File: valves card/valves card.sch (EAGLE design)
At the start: 68 parts, among them J1 09231486921, J2 TBP02R1-381-14BE, Q1 IRLZ44NSTRLPBF, Q11 IRLZ44NSTRLPBF, Q13 IRLZ44NSTRLPBF, Q15 IRLZ44NSTRLPBF, Q17 IRLZ44NSTRLPBF, Q19 IRLZ44NSTRLPBF, Q21 IRLZ44NSTRLPBF, Q23 IRLZ44NSTRLPBF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

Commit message: added cam data
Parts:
- Q1, Q11, Q13, Q15, Q17, Q19, Q21, Q23, Q3, Q5, Q7, Q9: device m_transistor:STD45NF75 -> BUK9214-30A,118:BUK9214-30A-118-DPAK
- U4: MP (none) -> OR-815
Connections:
- net 3.3V: now also U$1.VCC

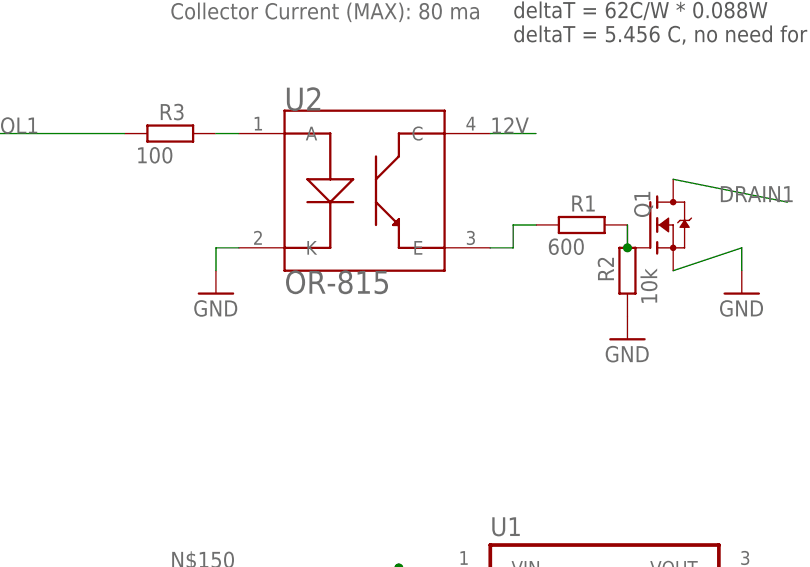
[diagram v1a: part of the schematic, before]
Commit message: added cam data, and ordered pcb's based on that cam data, will clean up repo next
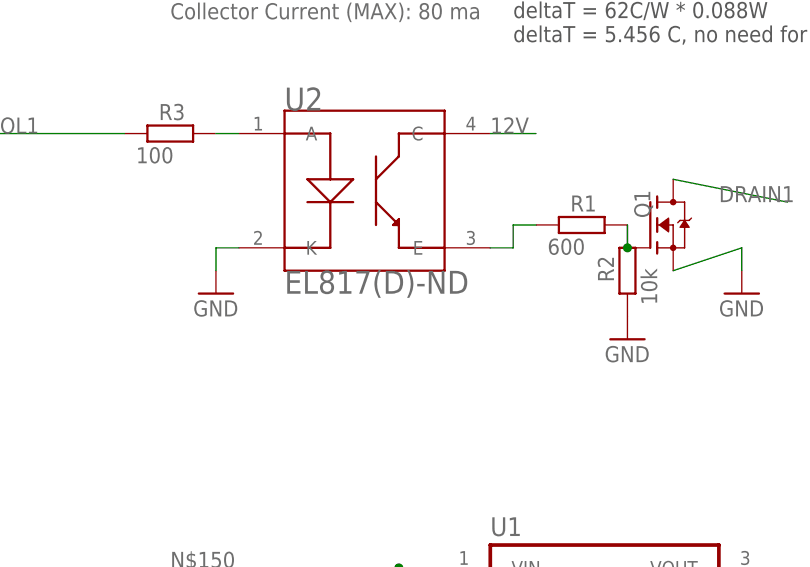
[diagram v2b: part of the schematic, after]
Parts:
- U2: value OR-815 -> EL817(D)-ND; BEST_I_COULD_FIND (none) -> EL817(D)-ND
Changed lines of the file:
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@@
 <part name="GND2" library="supply1" library_urn="urn:adsk.eagle:library:371" deviceset="GND" device=""/>
 <part name="GND3" library="supply1" library_urn="urn:adsk.eagle:library:371" deviceset="GND" device=""/>
-<part name="U2" library="EL817C" deviceset="EL817C" device="" value="OR-815">
+<part name="U2" library="EL817C" deviceset="EL817C" device="" value="EL817(D)-ND">
+<attribute name="BEST_I_COULD_FIND" value="EL817(D)-ND"/>
 <attribute name="MP" value="OR-815"/>
 </part>
@@
 <attribute name="NAME" x="208.26538125" y="45.73461875" size="2.54486875" layer="95"/>
 <attribute name="VALUE" x="208.26795" y="25.3799" size="2.54401875" layer="96"/>
+<attribute name="BEST_I_COULD_FIND" x="215.9" y="38.1" size="1.778" layer="96" display="off"/>
 </instance>
 <instance part="R1" gate="G$1" x="241.3" y="33.02" smashed="yes">

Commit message: added libraries
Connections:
- net N$150 renamed 24V
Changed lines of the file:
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@@
 </segment>
 </net>
-<net name="N$150" class="1">
+<net name="24V" class="1">
 <segment>
 <pinref part="J1" gate="G$1" pin="5"/>
